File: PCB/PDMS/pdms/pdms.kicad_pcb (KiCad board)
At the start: 2 copper layers, 152 parts, among them IC1 BTS500101TAEATMA1, IC12 TMP126NDCKR, IC13 TMP126NDCKR, IC14 TMP126NDCKR, IC15 LM74700MDDFREP, IC16 BTS722204ESAXUMA1, IC19 STM32L496ZGT6, IC2 BTS500101TAEATMA1, IC20 AT25SF128A-SHB-T, IC3 BTS500101TAEATMA1, IC4 BTS500101TAEATMA1, IC5 BTS500101TAEATMA1, IC6 BTS500101TAEATMA1, IC7 BTS722204ESAXUMA1, IC8 BTS500101TAEATMA1, IC9 BTS500101TAEATMA1, Q1 AO3401A, Q2 MMBT3904, Q3 IAUA250N04S6N007AUMA1, U2 MCP2561-E-SN, U3 MCP2561-E-SN, Y1 48Mhz, Y2 32KHz

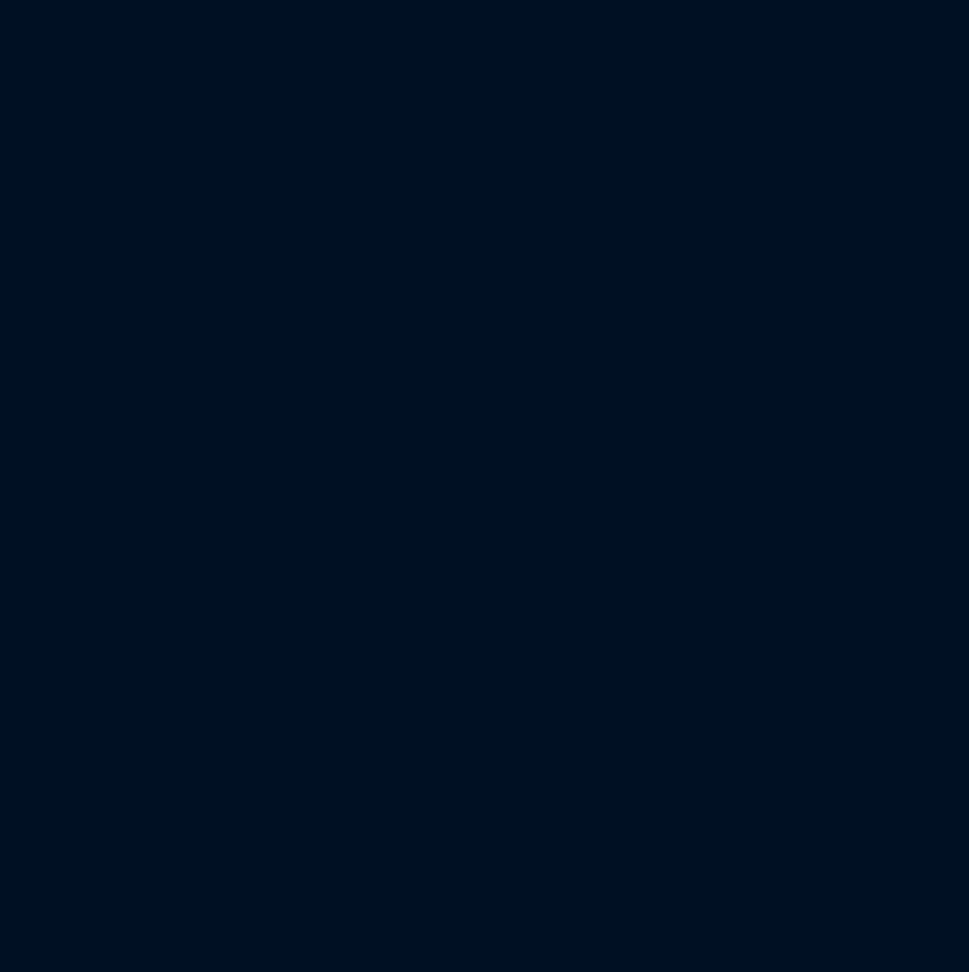
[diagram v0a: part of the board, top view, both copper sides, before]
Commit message: Changed power section symbol library
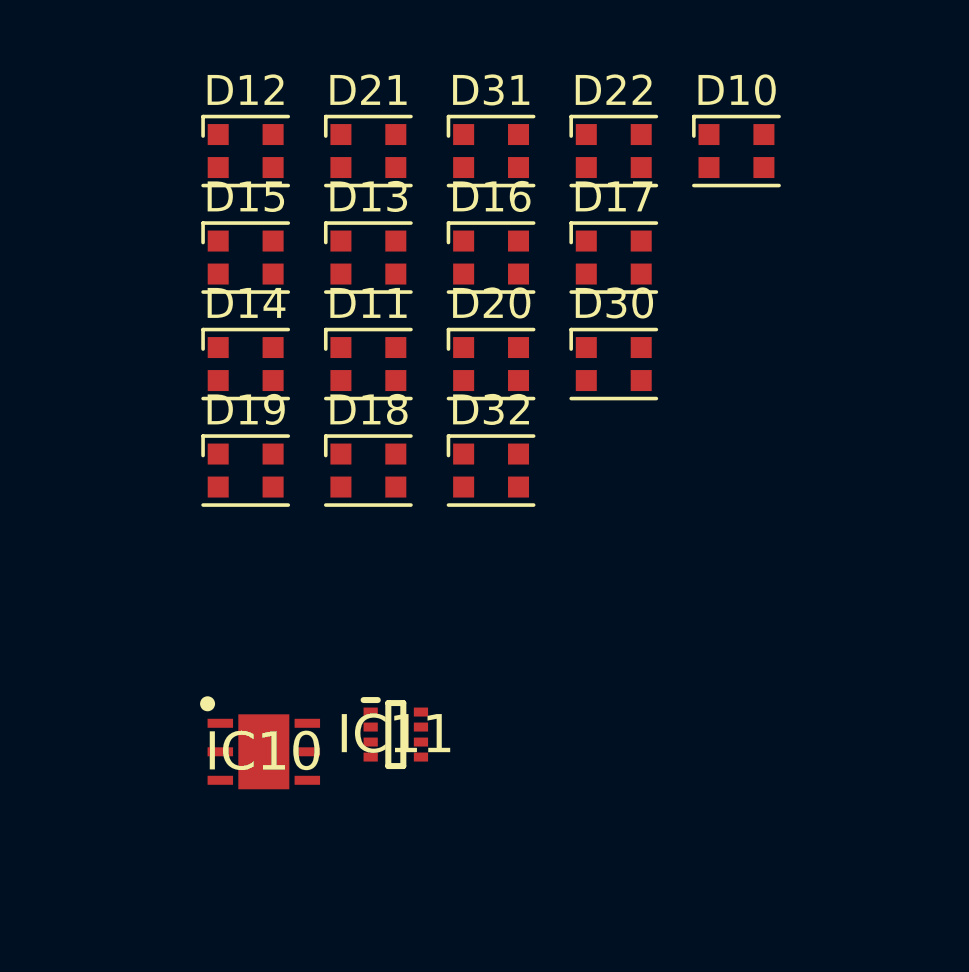
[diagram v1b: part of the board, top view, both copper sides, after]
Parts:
- added D10: WS2812B, LED_SMD:LED_WS2812B-2020_PLCC4_2.0x2.0mm, F.Cu at (114.3, 38.1)
- added D11: WS2812B, LED_SMD:LED_WS2812B-2020_PLCC4_2.0x2.0mm, F.Cu at (102.0, 45.2)
- added D12: WS2812B, LED_SMD:LED_WS2812B-2020_PLCC4_2.0x2.0mm, F.Cu at (97.9, 38.1)
- added D13: WS2812B, LED_SMD:LED_WS2812B-2020_PLCC4_2.0x2.0mm, F.Cu at (102.0, 41.6)
- added D14: WS2812B, LED_SMD:LED_WS2812B-2020_PLCC4_2.0x2.0mm, F.Cu at (97.9, 45.2)
- added D15: WS2812B, LED_SMD:LED_WS2812B-2020_PLCC4_2.0x2.0mm, F.Cu at (97.9, 41.6)
- added D16: WS2812B, LED_SMD:LED_WS2812B-2020_PLCC4_2.0x2.0mm, F.Cu at (106.1, 41.6)
- added D17: WS2812B, LED_SMD:LED_WS2812B-2020_PLCC4_2.0x2.0mm, F.Cu at (110.2, 41.6)
- added D18: WS2812B, LED_SMD:LED_WS2812B-2020_PLCC4_2.0x2.0mm, F.Cu at (102.0, 48.8)
- added D19: WS2812B, LED_SMD:LED_WS2812B-2020_PLCC4_2.0x2.0mm, F.Cu at (97.9, 48.8)
- added D20: WS2812B, LED_SMD:LED_WS2812B-2020_PLCC4_2.0x2.0mm, F.Cu at (106.1, 45.2)
- added D21: WS2812B, LED_SMD:LED_WS2812B-2020_PLCC4_2.0x2.0mm, F.Cu at (102.0, 38.1)
- added D22: WS2812B, LED_SMD:LED_WS2812B-2020_PLCC4_2.0x2.0mm, F.Cu at (110.2, 38.1)
- added D30: WS2812B, LED_SMD:LED_WS2812B-2020_PLCC4_2.0x2.0mm, F.Cu at (110.2, 45.2)
- added D31: WS2812B, LED_SMD:LED_WS2812B-2020_PLCC4_2.0x2.0mm, F.Cu at (106.1, 38.1)
- added D32: WS2812B, LED_SMD:LED_WS2812B-2020_PLCC4_2.0x2.0mm, F.Cu at (106.1, 48.8)
- added IC10: LDO40LPU50RY, PDMS_Additional:SON95P300X300X90-7N-D, F.Cu at (98.5, 58.1)
- added IC11: MP2332HGTL-P, PDMS_Additional:SOTFL50P160X60-8N, F.Cu at (102.9, 57.5)
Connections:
- F1 pad 1: +12V -> Net-(F1-Pad1)
- IC19 pad 117: unconnected-(IC19-Pad117) -> /PERIPHERAL/TEMP1_ALERT
- IC19 pad 118: unconnected-(IC19-Pad118) -> /PERIPHERAL/TEMP2_ALERT
- IC19 pad 119: unconnected-(IC19-Pad119) -> /PERIPHERAL/BUZZ_IN
- IC19 pad 70: unconnected-(IC19-Pad70) -> /ARGB_LEDS/LED_DATA_IN

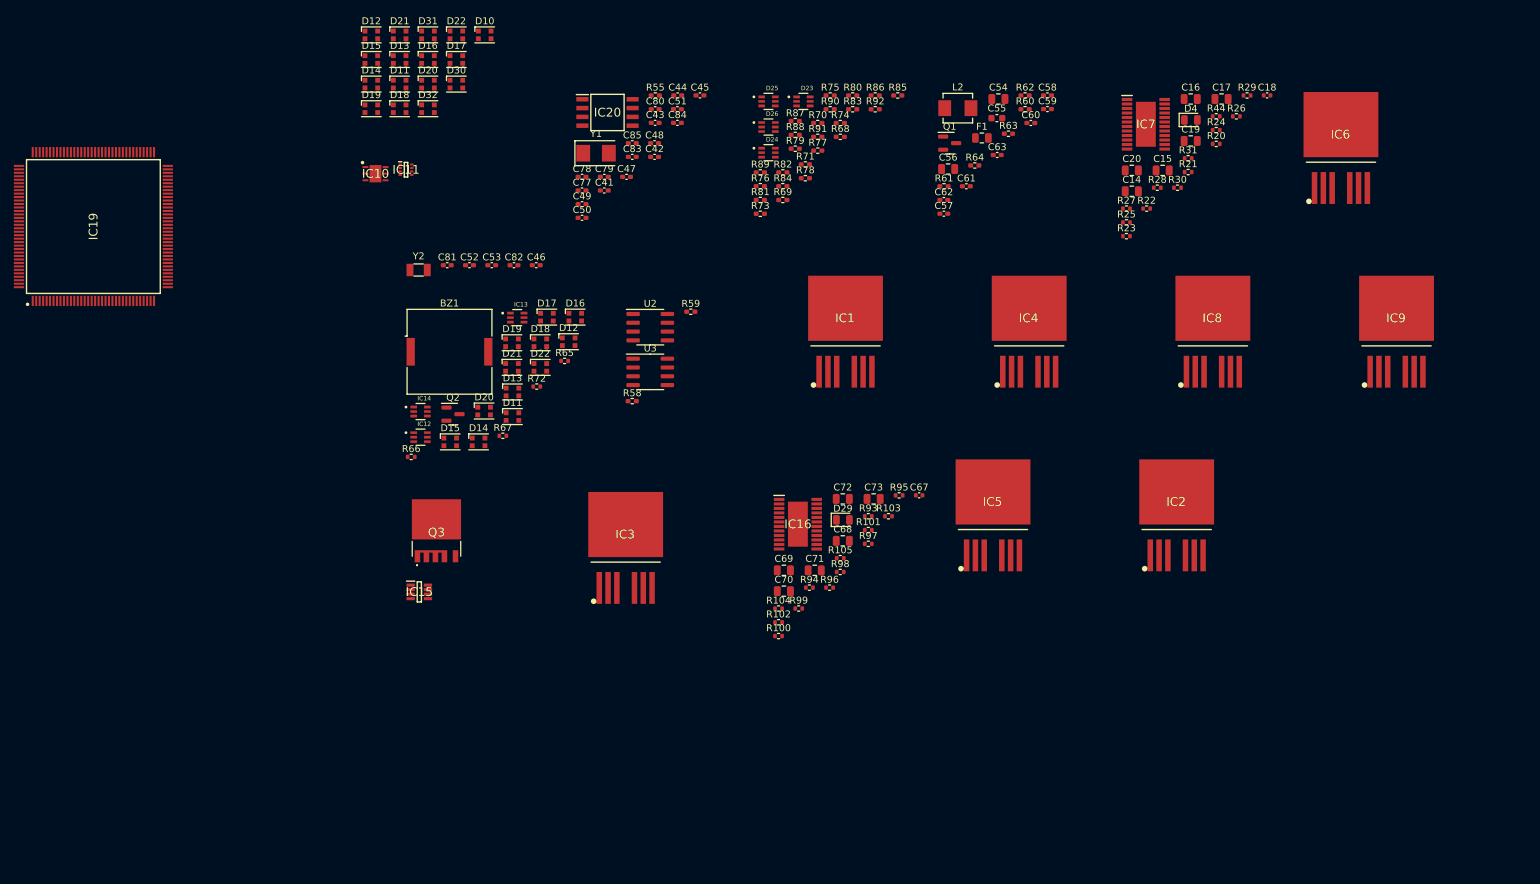
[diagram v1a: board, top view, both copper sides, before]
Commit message: Added input selection section and fusing
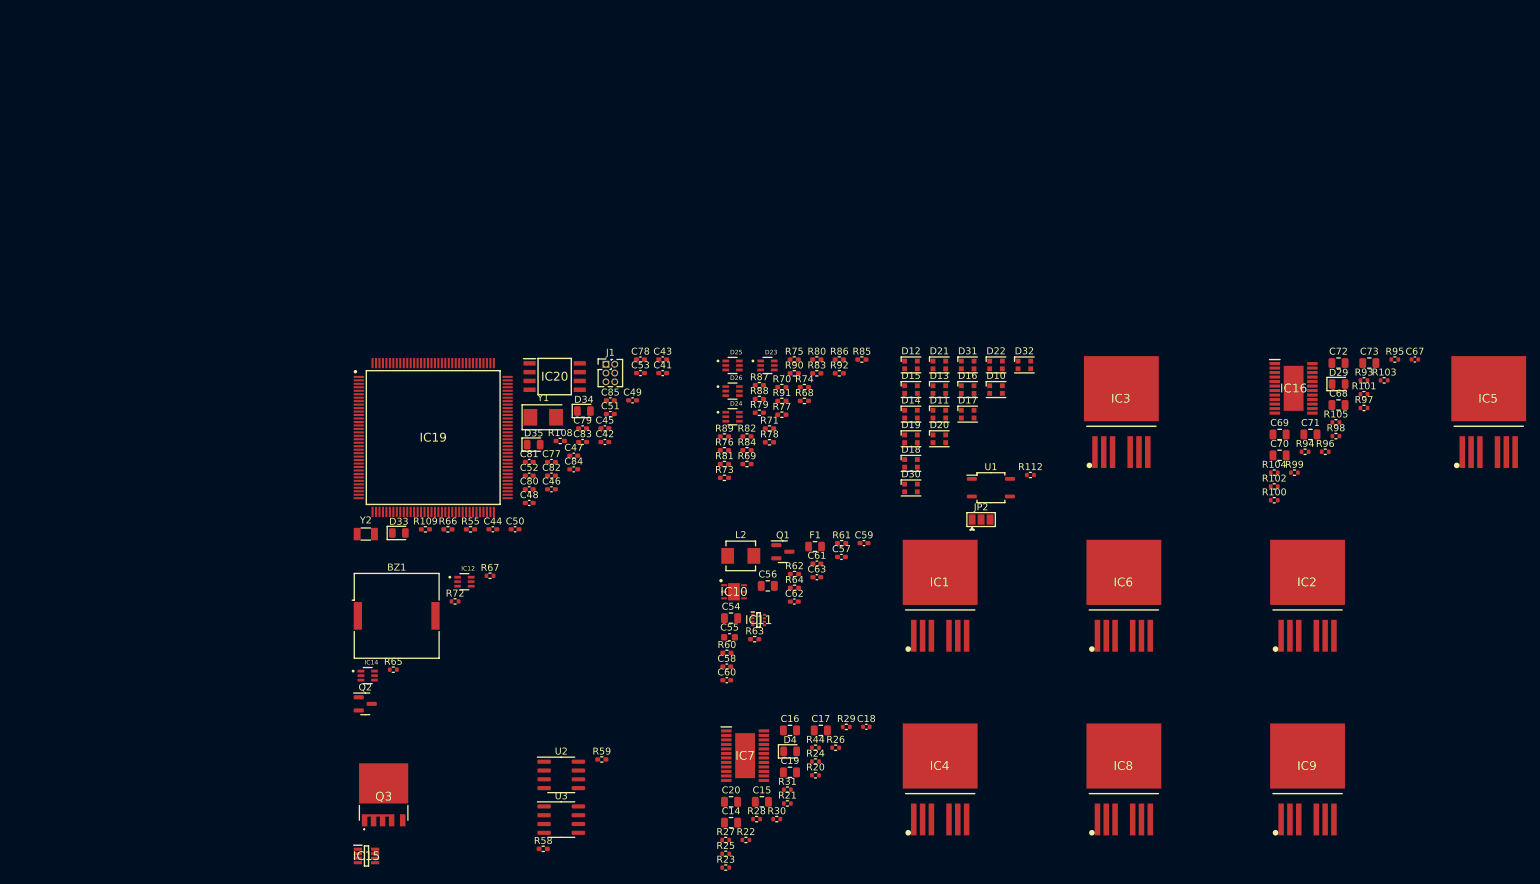
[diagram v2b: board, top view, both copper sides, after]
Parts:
- removed the D11 at (118.3, 93.2)
- removed the D11 at (102.0, 45.2)
- removed the D12 at (97.9, 38.1)
- removed the D12 at (126.4, 82.4)
- removed the D13 at (118.3, 89.6)
- removed the D13 at (102.0, 41.6)
- removed the D14 at (97.9, 45.2)
- removed the D14 at (113.4, 96.8)
- removed the D15 at (97.9, 41.6)
- removed the D15 at (109.3, 96.8)
- removed the D16 at (127.4, 78.8)
- removed the D16 at (106.1, 41.6)
- removed the D17 at (110.2, 41.6)
- removed the D17 at (123.3, 78.8)
- removed the D18 at (122.3, 82.5)
- removed the D18 at (102.0, 48.8)
- removed the D19 at (118.2, 82.5)
- removed the D19 at (97.9, 48.8)
- removed the D20 at (106.1, 45.2)
- removed the D20 at (114.2, 92.4)
- removed the D21 at (118.2, 86.1)
- removed the D21 at (102.0, 38.1)
- removed the D22 at (110.2, 38.1)
- removed the D22 at (122.3, 86.1)
- removed IC13: TMP126NDCKR, PDM_Additional:SOT65P210X110-6N
- added D11: WS2812B, LED_SMD:LED_WS2812B-2020_PLCC4_2.0x2.0mm, F.Cu at (179.9, 92.8)
- added D12: WS2812B, LED_SMD:LED_WS2812B-2020_PLCC4_2.0x2.0mm, F.Cu at (175.8, 85.7)
- added D13: WS2812B, LED_SMD:LED_WS2812B-2020_PLCC4_2.0x2.0mm, F.Cu at (179.9, 89.3)
- added D14: WS2812B, LED_SMD:LED_WS2812B-2020_PLCC4_2.0x2.0mm, F.Cu at (175.8, 92.8)
- added D15: WS2812B, LED_SMD:LED_WS2812B-2020_PLCC4_2.0x2.0mm, F.Cu at (175.8, 89.3)
- added D16: WS2812B, LED_SMD:LED_WS2812B-2020_PLCC4_2.0x2.0mm, F.Cu at (184.0, 89.3)
- added D17: WS2812B, LED_SMD:LED_WS2812B-2020_PLCC4_2.0x2.0mm, F.Cu at (184.0, 92.8)
- added D18: WS2812B, LED_SMD:LED_WS2812B-2020_PLCC4_2.0x2.0mm, F.Cu at (175.8, 99.9)
- added D19: WS2812B, LED_SMD:LED_WS2812B-2020_PLCC4_2.0x2.0mm, F.Cu at (175.8, 96.4)
- added D20: WS2812B, LED_SMD:LED_WS2812B-2020_PLCC4_2.0x2.0mm, F.Cu at (179.9, 96.4)
- added D21: WS2812B, LED_SMD:LED_WS2812B-2020_PLCC4_2.0x2.0mm, F.Cu at (179.9, 85.7)
- added D22: WS2812B, LED_SMD:LED_WS2812B-2020_PLCC4_2.0x2.0mm, F.Cu at (188.1, 85.7)
- added D33: LED, LED_SMD:LED_0805_2012Metric, F.Cu at (101.9, 110.0)
- added D34: LED, LED_SMD:LED_0805_2012Metric, F.Cu at (128.6, 92.4)
- added D35: LED, LED_SMD:LED_0805_2012Metric, F.Cu at (121.4, 97.2)
- added J1: DBG, Connector_PinHeader_1.27mm:PinHeader_2x03_P1.27mm_Vertical, F.Cu at (131.8, 85.6)
- added JP2: IN_SEL, Jumper:SolderJumper-3_P1.3mm_Open_Pad1.0x1.5mm, F.Cu at (185.9, 108.0)
- added R108: 1k5, Resistor_SMD:R_0402_1005Metric_Pad0.72x0.64mm_HandSolder, F.Cu at (125.2, 96.7)
- added R109: 1k5, Resistor_SMD:R_0402_1005Metric_Pad0.72x0.64mm_HandSolder, F.Cu at (105.7, 109.4)
- added R112: 1k, Resistor_SMD:R_0402_1005Metric, F.Cu at (193.0, 101.6)
- added U1: CPC1117N, Package_SO:SOP-4_3.8x4.1mm_P2.54mm, F.Cu at (187.3, 103.4)
- R66: value 10k -> 1k5; footprint Resistor_SMD:R_0402_1005Metric -> Resistor_SMD:R_0402_1005Metric_Pad0.72x0.64mm_HandSolder
- moved C18 107.9 mm to (169.4, 137.9)
- moved R20 107.9 mm to (162.0, 144.9)
- moved R21 107.9 mm to (158.0, 149.0)
- moved R23 107.9 mm to (149.1, 158.2)
- moved C14 107.9 mm to (149.8, 151.8)
- moved C15 107.9 mm to (154.3, 148.8)
- moved C16 107.9 mm to (158.3, 138.4)
- moved C17 107.9 mm to (162.8, 138.4)
- moved C19 107.9 mm to (158.3, 144.5)
- moved C20 107.9 mm to (149.8, 148.8)
- moved D4 107.9 mm to (158.4, 141.5)
- moved IC7 107.9 mm to (151.9, 142.1)
- moved R22 107.9 mm to (152.0, 154.3)
- moved R24 107.9 mm to (162.0, 142.9)
- moved R25 107.9 mm to (149.1, 156.2)
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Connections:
- net HP_MOS1 renamed /POWER_SWITCHES/BTS50010-1TAE/MOS_OUT
- net HP_MOS2 renamed /POWER_SWITCHES/BTS50010-1TAE1/MOS_OUT
- net HP_MOS3 renamed /POWER_SWITCHES/BTS50010-1TAE2/MOS_OUT
- net HP_MOS4 renamed /POWER_SWITCHES/BTS50010-1TAE3/MOS_OUT
- net HP_MOS5 renamed /POWER_SWITCHES/BTS50010-1TAE4/MOS_OUT
- net HP_MOS6 renamed /POWER_SWITCHES/BTS50010-1TAE6/MOS_OUT
- net LP_MOS1 renamed /POWER_SWITCHES/BTS722204/OUT0
- net LP_MOS2 renamed /POWER_SWITCHES/BTS722204/OUT1
- net LP_MOS3 renamed /POWER_SWITCHES/BTS722204/OUT2
- net LP_MOS4 renamed /POWER_SWITCHES/BTS722204/OUT3
- net LP_MOS5 renamed /POWER_SWITCHES/BTS722205/OUT0
- net LP_MOS6 renamed /POWER_SWITCHES/BTS722205/OUT1
- net LP_MOS7 renamed /POWER_SWITCHES/BTS722205/OUT2
- net LP_MOS8 renamed /POWER_SWITCHES/BTS722205/OUT3
- net SIG_IN1 renamed PWM_SIG1
- net SIG_IN2 renamed PWM_SIG2
- net SIG_IN3 renamed PWM_SIG3
- net SIG_IN4 renamed PWM_SIG4
- net SIG_IN5 renamed PWM_SIG5
- net SIG_IN6 renamed PWM_SIG6
- net SIG_IN7 renamed PWM_SIG7
- net SIG_IN8 renamed PWM_SIG8
- IC19 pad 1: unconnected-(IC19-Pad1) -> LED_STATUS
- IC19 pad 105: /SWDIO -> SWDIO
- IC19 pad 109: /SWCLK -> SWCLK
- IC19 pad 25: unconnected-(IC19-Pad25) -> NRST
- IC8 pad 5: HP_MOS7 -> /POWER_SWITCHES/BTS50010-1TAE7/MOS_OUT
- IC8 pad 6: HP_MOS7 -> /POWER_SWITCHES/BTS50010-1TAE7/MOS_OUT
- IC8 pad 7: HP_MOS7 -> /POWER_SWITCHES/BTS50010-1TAE7/MOS_OUT
- IC9 pad 5: HP_MOS7 -> /POWER_SWITCHES/BTS50010-1TAE5/MOS_OUT
- IC9 pad 6: HP_MOS7 -> /POWER_SWITCHES/BTS50010-1TAE5/MOS_OUT
- IC9 pad 7: HP_MOS7 -> /POWER_SWITCHES/BTS50010-1TAE5/MOS_OUT
- R66 pad 1: VDD -> LED_STATUS
- R66 pad 2: TEMP1_ALERT -> Net-(D33-Pad2)
